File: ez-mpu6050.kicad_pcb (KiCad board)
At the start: 2 copper layers, 20.5 x 29.1 mm, 25 parts, among them J1 I2C, J3 Conn_01x06, J4 Conn_01x06, J5 I2C, U1 MPU-6050, U2 AP2112K-3.3

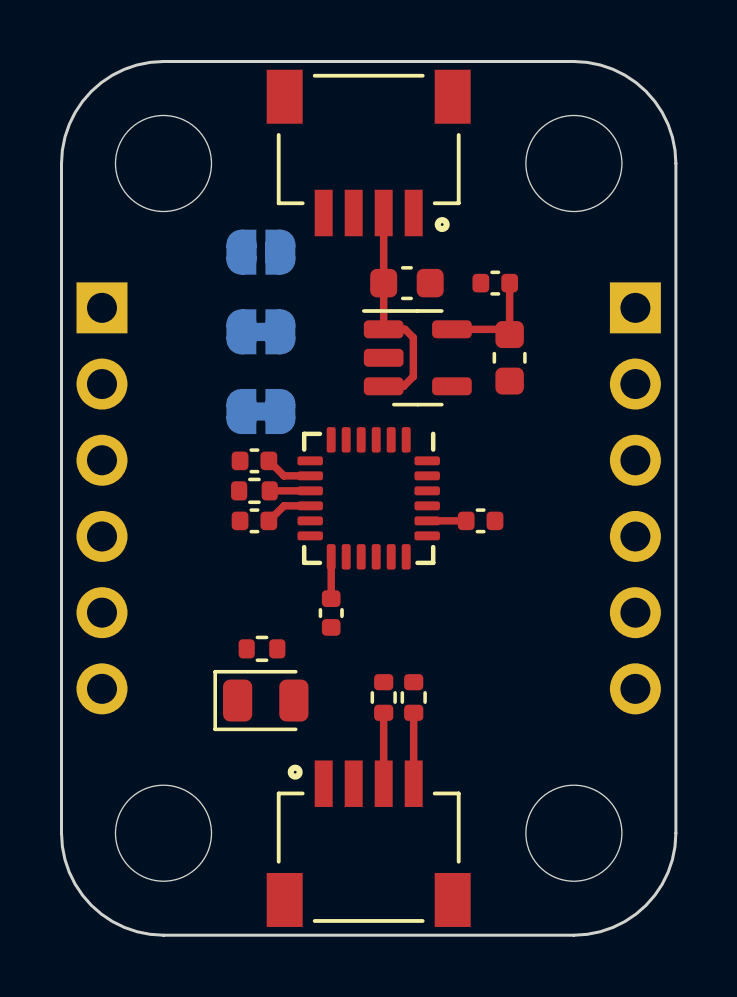
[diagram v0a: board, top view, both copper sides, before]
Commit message: Finish tracks add zone & GND vias
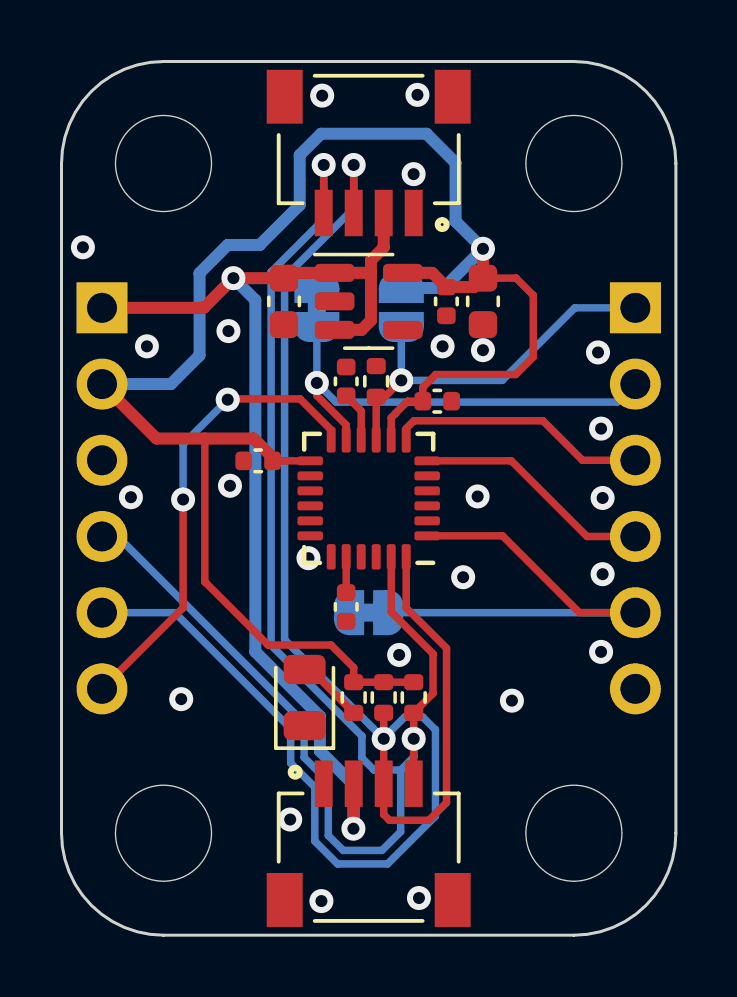
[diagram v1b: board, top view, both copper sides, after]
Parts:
- moved JP2 10.0 mm to (171.9, 119.7), turned to 0 degrees
- moved C1 6.41 mm to (174.1, 112.7), turned to 0 degrees
- moved C4 5.63 mm to (168.2, 114.7), turned to 180 degrees
- moved C2 5.56 mm to (171.1, 112.0), turned to 90 degrees
- moved R3 5.46 mm to (172.1, 112.0), turned to 90 degrees
- moved C3 5.32 mm to (171.1, 119.6), turned to -90 degrees
- moved JP1 5.03 mm to (172.9, 109.6), turned to 90 degrees
- moved C5 4.14 mm to (169.0, 109.4), turned to -90 degrees
- moved JP3 3.94 mm to (170.1, 109.6), turned to -90 degrees
- moved R4 3.46 mm to (171.4, 122.6), turned to -90 degrees
- moved U2 2.49 mm to (171.9, 109.4)
- moved C6 2.08 mm to (175.7, 109.4)
- moved C7 1.74 mm to (174.4, 109.4), turned to -90 degrees
- moved D1 1.30 mm to (169.7, 122.6), turned to 90 degrees
- turned U1 to 180 degrees
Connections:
- J3 pad 1: VDD -> /AD0
- J3 pad 2: +3V3 -> /FSYNC_IN
- J3 pad 3: GND -> /SCL_EXT
- J3 pad 4: /SCL -> /SDA_EXT
- J3 pad 5: /SDA -> /CLKIN
- J3 pad 6: /INT -> GND
- J4 pad 1: /AD0 -> VDD
- J4 pad 2: /FSYNC_IN -> +3V3
- J4 pad 3: /SCL_EXT -> GND
- J4 pad 4: /SDA_EXT -> /SCL
- J4 pad 5: /CLKIN -> /SDA
- J4 pad 6: GND -> /INT
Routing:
- net /SDA: track 2.36 -> 59.7 mm, vias 0 -> 2
- net +3V3: track 6.69 -> 60.7 mm, vias 0 -> 1
- net /SCL: track 2.36 -> 52.8 mm, vias 0 -> 2
- net VDD: track 7.40 -> 36.1 mm, vias 0 -> 2
- net /CLKIN: track 0.00 -> 16.2 mm
- net /INT: track 0.00 -> 15.6 mm, vias 0 -> 2
- net /FSYNC_IN: track 0.00 -> 15.3 mm, vias 0 -> 1
- net /AD0: track 1.35 -> 13.1 mm, vias 0 -> 1
- net /SCL_EXT: track 0.00 -> 8.67 mm
- net /SDA_EXT: track 0.00 -> 7.98 mm
- net Net-(D1-A): track 0.00 -> 2.23 mm
- net GND: vias 0 -> 24

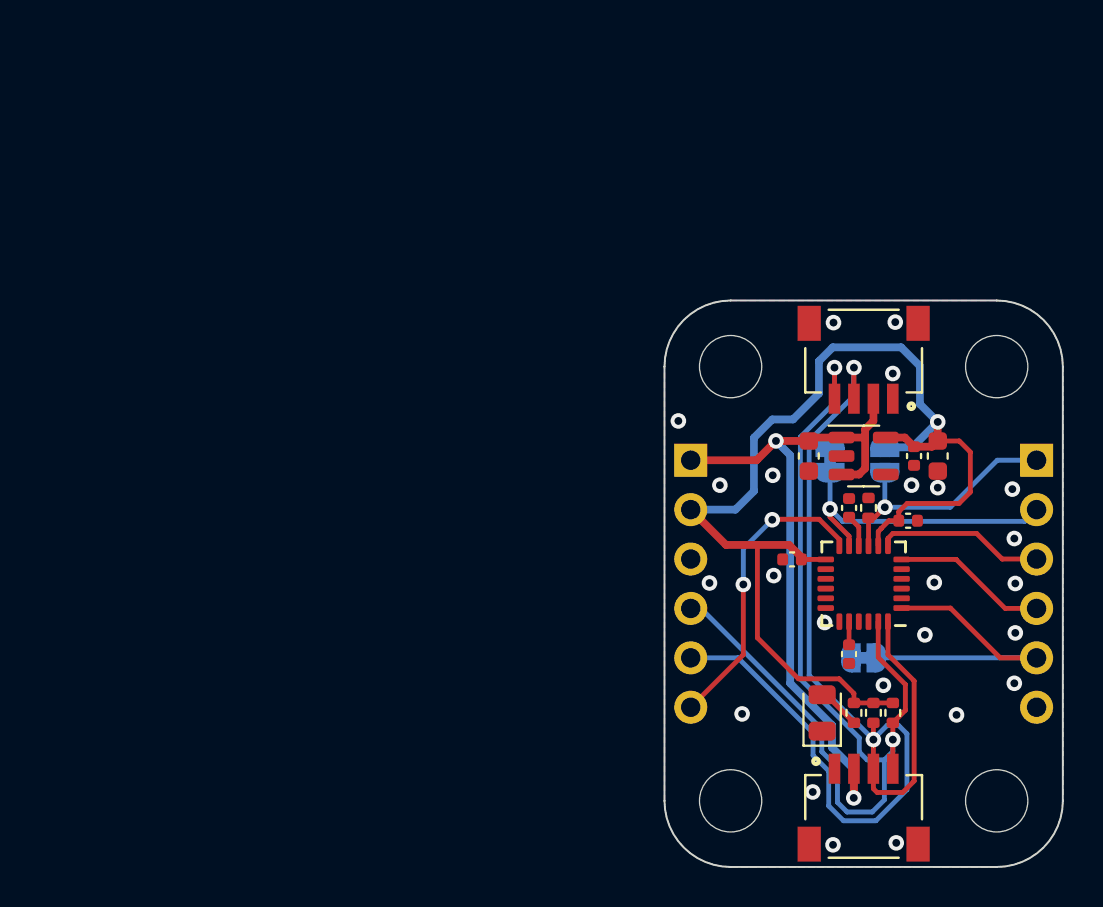
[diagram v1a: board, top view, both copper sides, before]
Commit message: Add RPU enable jumper
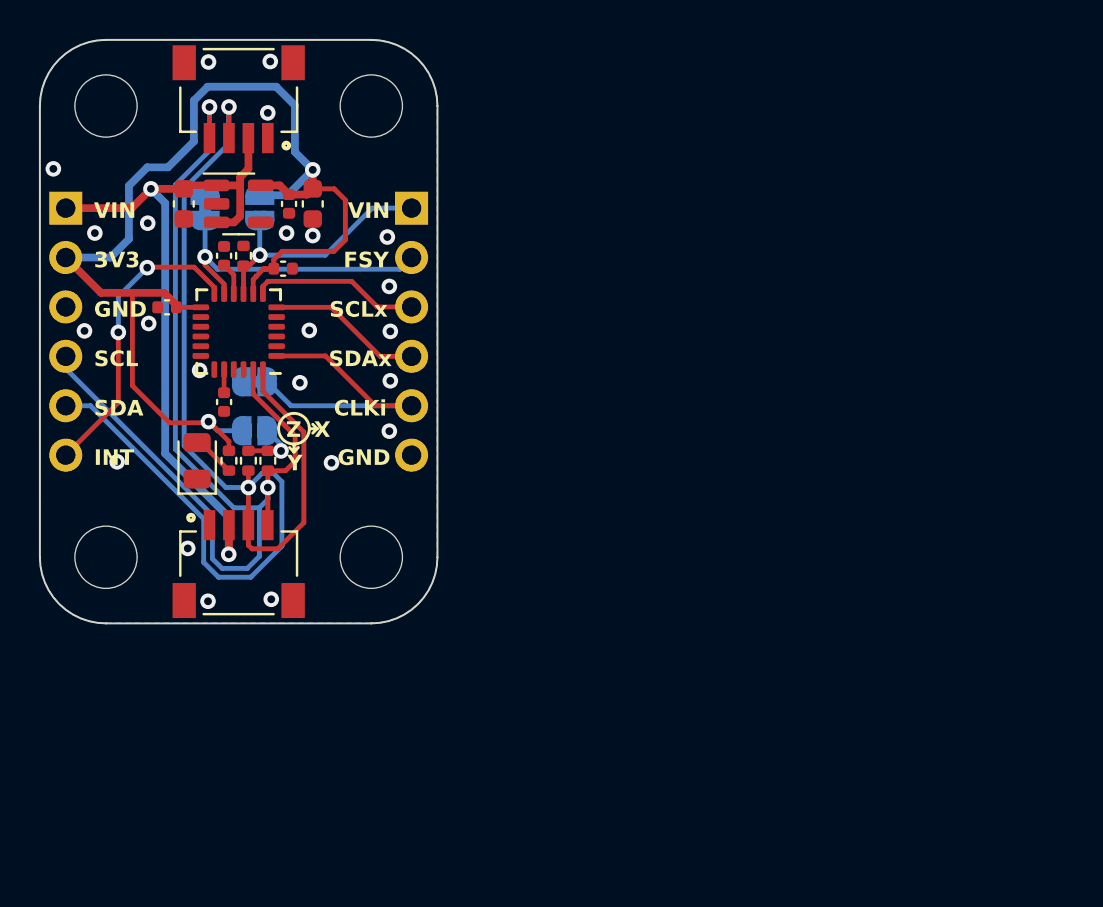
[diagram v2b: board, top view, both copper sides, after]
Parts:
- added JP4: JMP, Jumper:SolderJumper-2_P1.3mm_Open_RoundedPad1.0x1.5mm, B.Cu at (140.5, 108.1)
- moved H1 34.8 mm to (146.5, 91.4)
- moved J1 34.8 mm to (139.7, 93.0)
- moved H2 34.8 mm to (132.9, 91.4)
- moved C2 34.6 mm to (139.0, 99.1)
- moved C3 34.6 mm to (139.0, 106.6)
- moved C5 34.6 mm to (136.9, 96.4)
- moved C6 34.6 mm to (143.5, 96.4)
- moved C7 34.6 mm to (142.3, 96.4)
- moved J3 34.6 mm to (148.6, 96.6)
- moved J4 34.6 mm to (130.8, 96.6)
- moved R1 34.6 mm to (140.2, 109.6)
- moved R2 34.6 mm to (141.2, 109.6)
- moved R3 34.6 mm to (140.0, 99.1)
- moved R4 34.6 mm to (139.2, 109.6)
- moved U2 34.6 mm to (139.7, 96.4)
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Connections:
- R1 pad 1: +3V3 -> Net-(JP4-A)
- R2 pad 1: +3V3 -> Net-(JP4-A)
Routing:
- net Net-(JP4-A): track 0.00 -> 3.02 mm, vias 0 -> 1
- net /SCL: track 52.8 -> 55.6 mm
- net /SDA: track 59.7 -> 62.5 mm
- net +3V3: track 60.7 -> 61.6 mm, vias 1 -> 2
- net VDD: track 36.1 -> 36.9 mm
- net GND: vias 24 -> 23
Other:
- board size 20.5 x 29.1 mm -> 20.4 x 30 mm
- board text added: "3V3"
- board text added: "ADD"
- board text added: "CLK"
- board text added: "CLKi"
- board text added: "FSY"
- board text added: "GND"
- board text added: "INT"
- board text added: "RPU"
- board text added: "SCL"
- board text added: "SCLx"
- board text added: "SDA"
- board text added: "SDAx"
- board text added: "VIN"
- board text added: "X"
- board text added: "Y"
- board text added: "Z"
